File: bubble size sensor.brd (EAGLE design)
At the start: 91.4 x 72.9 mm, 44 parts, among them P5 TPPAD1-13, P6 TPPAD1-13, P7 TPPAD1-13, U1 PINHD-1X6

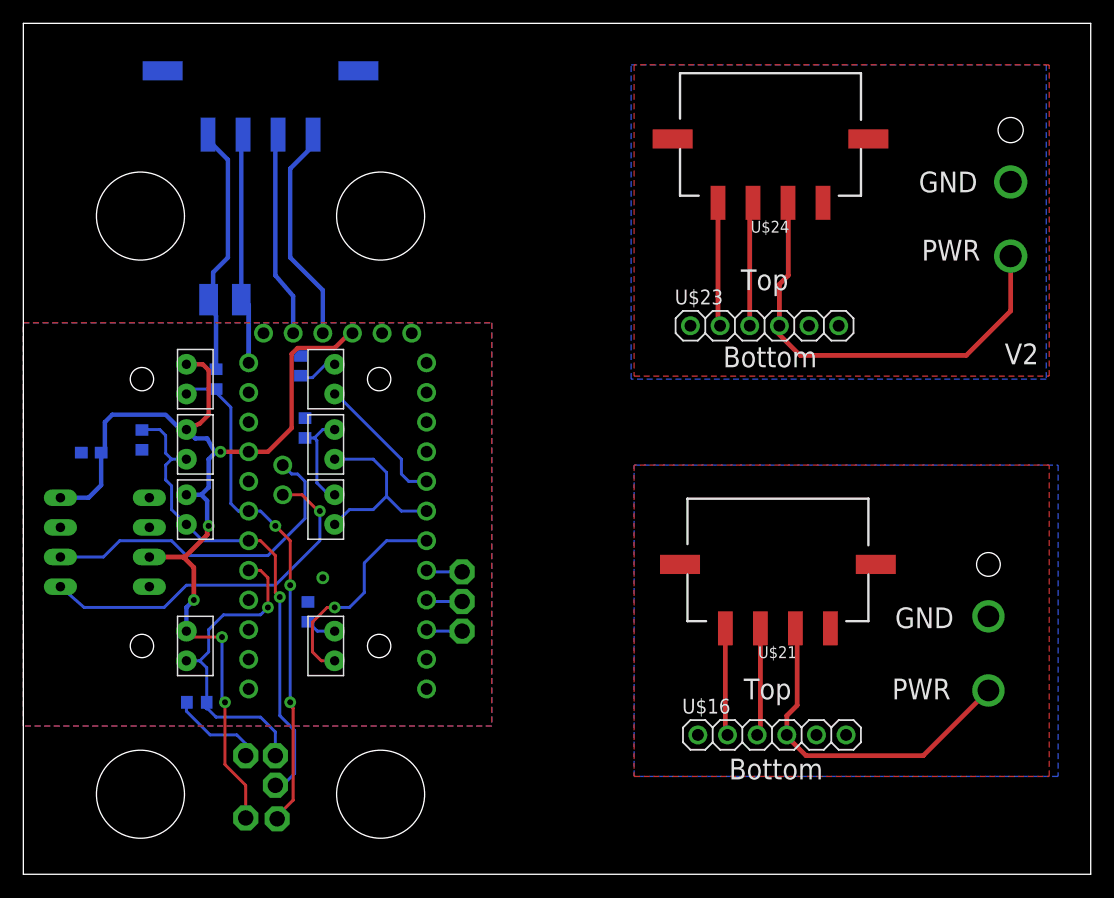
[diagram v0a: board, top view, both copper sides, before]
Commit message: Schematic updated with new EEPROMs
Board layout still in progress.
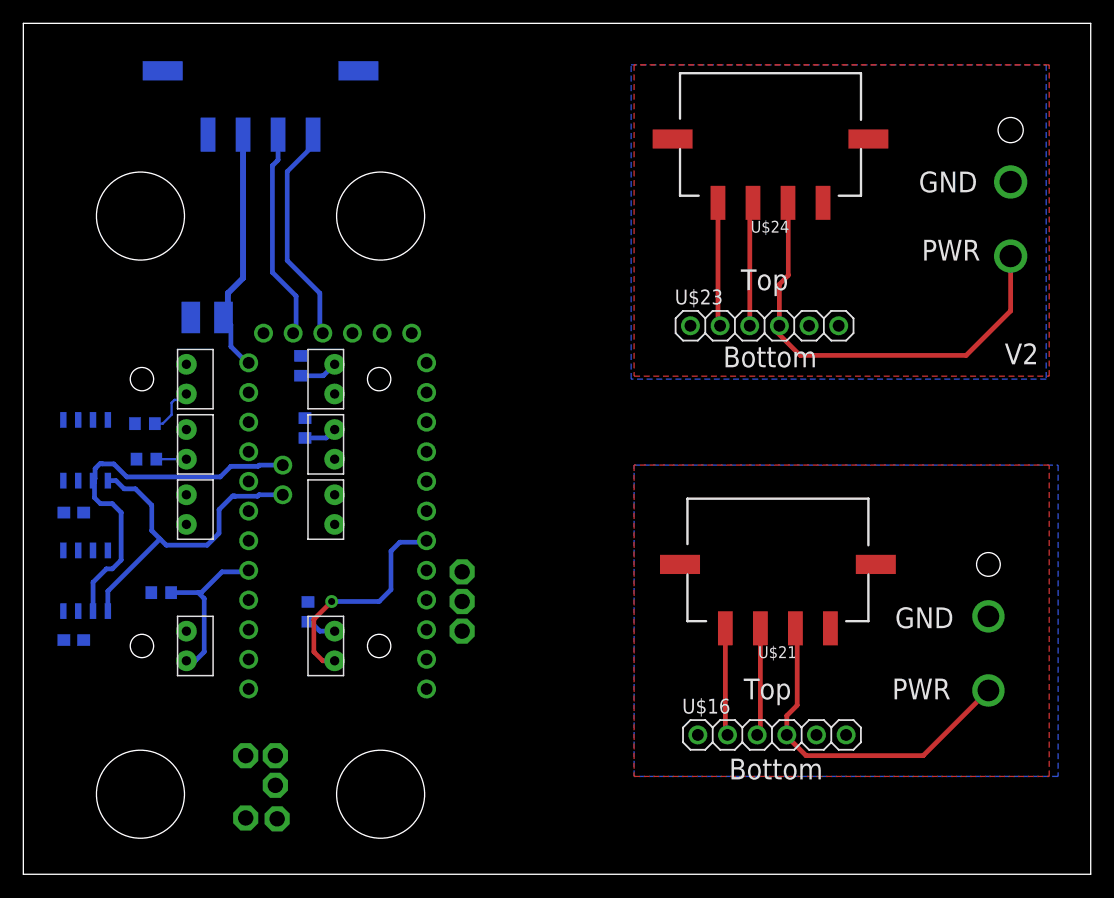
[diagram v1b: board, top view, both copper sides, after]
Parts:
- removed IC1: (no value), ic-package:DIL08
- added C3: (no value), rcl:C0603
- added U2, U3: M24M02-DR-1, Schuyler:SO8N
- moved R6 9.88 mm to (11.8, 24.1)
- moved R4 7.19 mm to (10.4, 38.6), turned to 0 degrees
- moved C1 5.35 mm to (4.32, 31.0), turned to 180 degrees
- moved C2 2.16 mm to (15.7, 47.7)
- moved R5 1.69 mm to (10.5, 35.6), turned to 0 degrees
- renumbered U$12 to H$12, U$13 to H$13, U$15 to H$15, U$17 to H$17, U$18 to H$18, U$19 to H$19, U$20 to H$20
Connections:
- net A4: now also U2.P$5, U3.P$5; no longer IC1.5
- net A5: now also U2.P$6, U3.P$6; no longer IC1.6
- net GND: now also C3.2, U2.P$3, U2.P$4, U2.P$7, U3.P$4, U3.P$7; no longer IC1.1, IC1.2, IC1.4, IC1.7
- net VCC: now also C3.1, U2.P$8, U3.P$3, U3.P$8; no longer IC1.3, IC1.8
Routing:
- net VCC: track 90.2 -> 0.00 mm, vias 5 -> 0
- net A1: track 42.6 -> 2.58 mm, vias 1 -> 0
- net A2: track 44.0 -> 4.35 mm, vias 3 -> 0
- net GND: track 30.1 -> 0.00 mm, vias 1 -> 0
- net 3: track 16.3 -> 0.00 mm
- net A0: track 27.5 -> 14.6 mm, vias 1 -> 0
- net 2: track 11.7 -> 0.00 mm
- net N$2: track 8.72 -> 2.84 mm
- net A5: track 29.0 -> 32.3 mm
- net 6: track 3.10 -> 0.00 mm
- net 7: track 3.10 -> 0.00 mm
- net 5: track 3.10 -> 0.00 mm
- net A4: track 31.6 -> 29.6 mm, vias 1 -> 0
- net N$6: track 20.0 -> 21.2 mm
- removed copper zone on layer 1, net GND
- removed copper zone on layer 16, net GND

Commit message: Board layout finished
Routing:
- net VCC: track 0.00 -> 96.9 mm, vias 0 -> 6
- net A2: track 4.35 -> 50.0 mm, vias 0 -> 1
- net A1: track 2.58 -> 41.2 mm, vias 0 -> 2
- net 2: track 0.00 -> 13.1 mm
- net A0: track 14.6 -> 27.3 mm, vias 0 -> 1
- net A5: track 32.3 -> 44.3 mm
- net 3: track 0.00 -> 8.35 mm
- net N$2: track 2.84 -> 8.98 mm
- net A4: track 29.6 -> 33.6 mm
- net 6: track 0.00 -> 3.10 mm
- net 7: track 0.00 -> 3.10 mm
- net 5: track 0.00 -> 3.10 mm
- net GND: track 0.00 -> 2.20 mm, vias 0 -> 2
- net 4: track 19.3 -> 18.0 mm
- net N$7: track 18.2 -> 17.5 mm
- added copper zone on layer 1, net GND
- added copper zone on layer 16, net GND
